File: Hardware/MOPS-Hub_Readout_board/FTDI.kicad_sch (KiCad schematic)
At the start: 44 parts, among them J1 USB_C_Receptacle_USB2.0_14P, U1 TPS73633DBV, U2 93LCxxB, U3 FT2232HL, Y1 12MHz

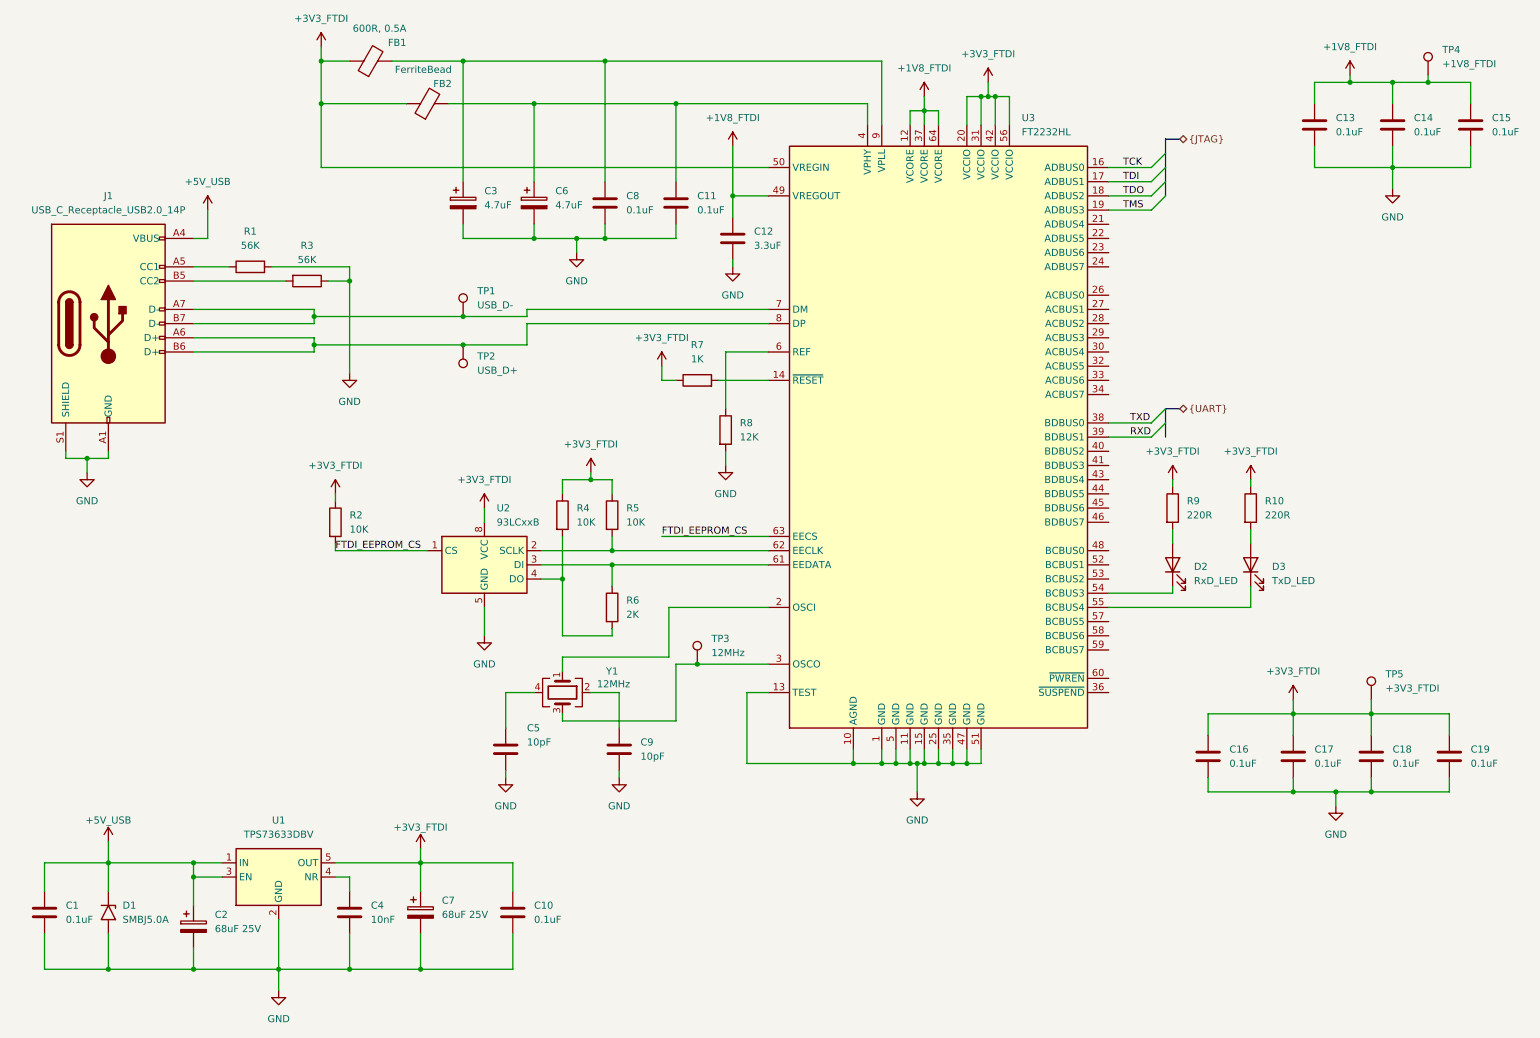
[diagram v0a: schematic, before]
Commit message: #8: incorporated comparator IC for Power-on-JTAG
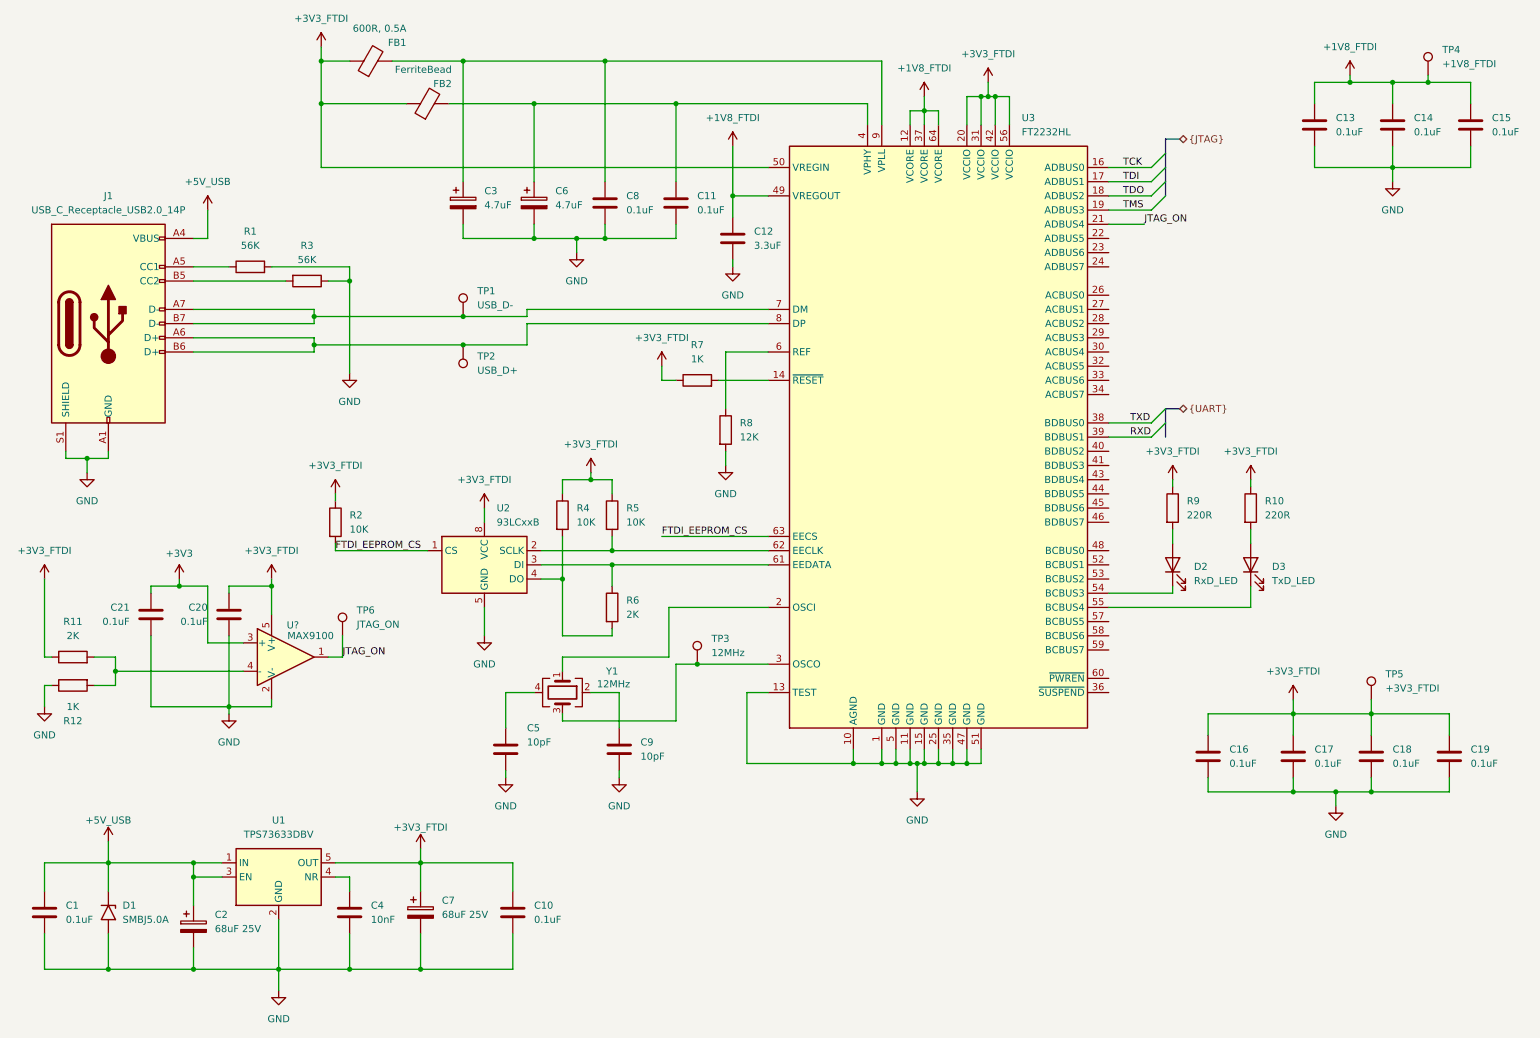
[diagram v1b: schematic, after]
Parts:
- added C20, C21: 0.1uF, Capacitor_SMD:C_0805_2012Metric, symbol Device:C
- added R11: 2K, Resistor_SMD:R_0805_2012Metric, symbol Device:R
- added R12: 1K, Resistor_SMD:R_0805_2012Metric, symbol Device:R
- added TP6: JTAG_ON, symbol Connector:TestPoint
- added U?: MAX9100, Package_TO_SOT_SMD:SOT-23-5, symbol ReadoutBoard_Simbols:MAX9100
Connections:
- net +3V3_FTDI: now also C20.1, R11.1, U?.5 (V+)
- net GND: now also C20.2, C21.2, R12.1, U?.2 (V-)
- net JTAG_ON: now reaches U3.21 (ADBUS4)
- net JTAG_ON: now also TP6.1, U?.1
- new net: R11.2, R12.2, U?.4 (-)
- new net +3V3: C21.1, U?.3 (+)
